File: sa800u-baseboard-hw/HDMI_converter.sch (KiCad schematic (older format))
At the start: 17 parts

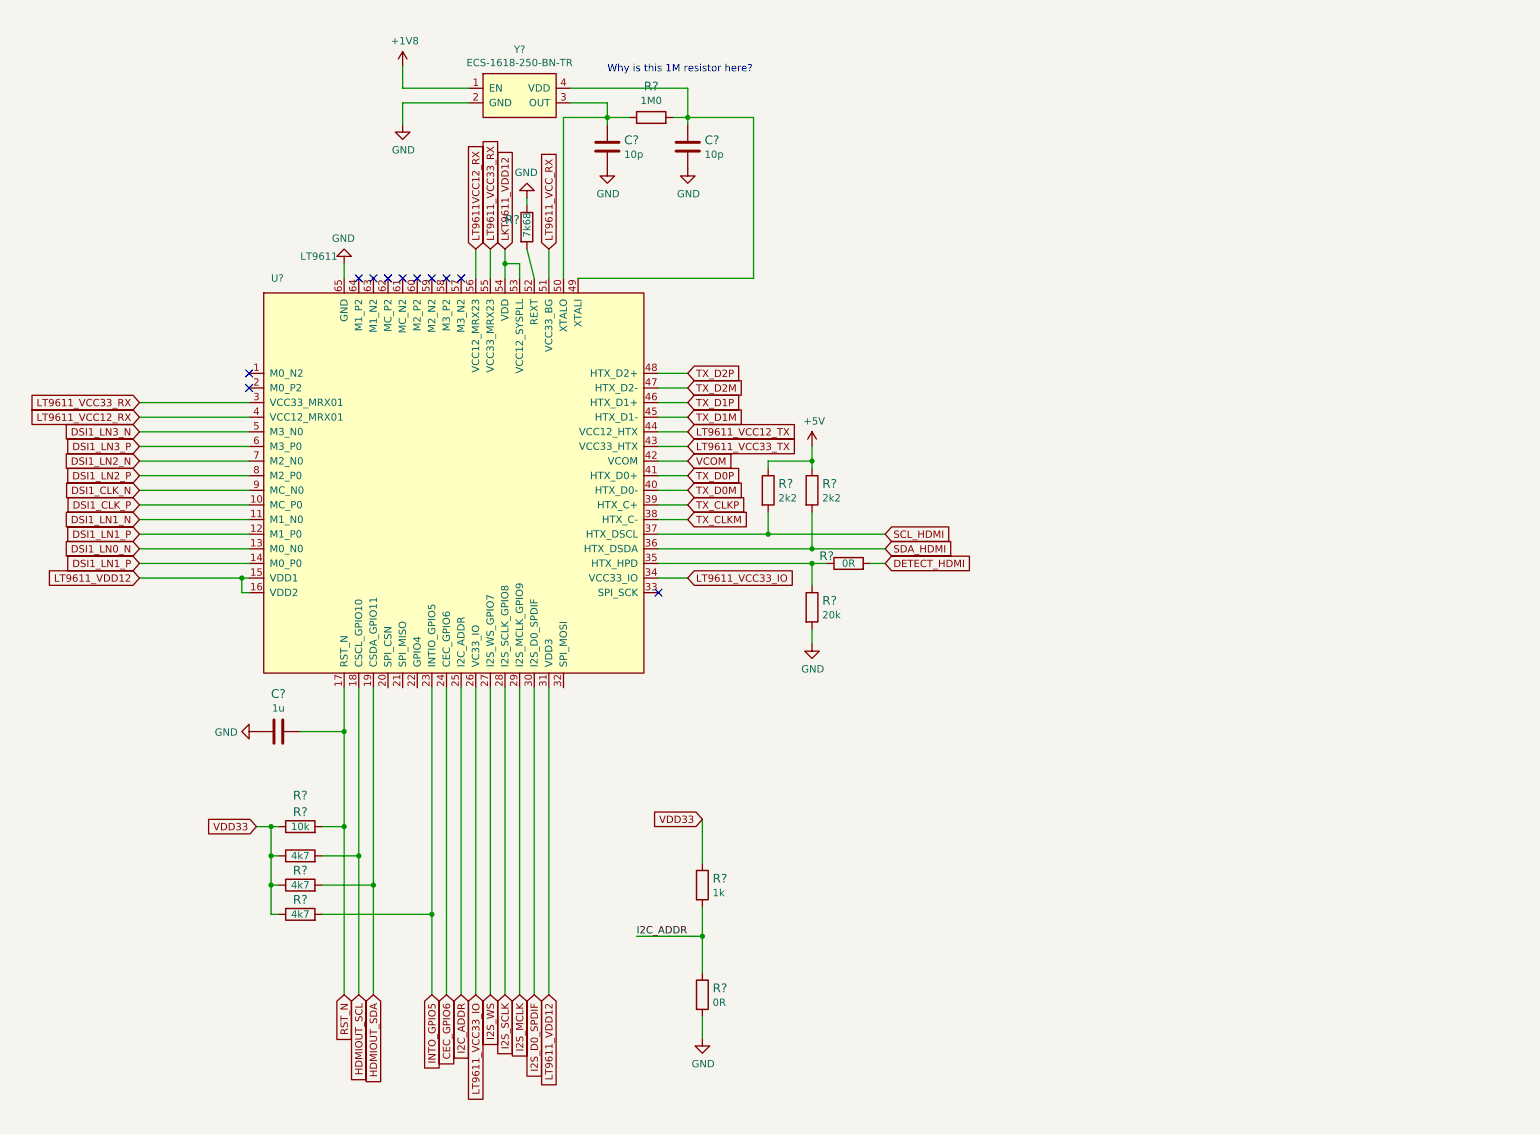
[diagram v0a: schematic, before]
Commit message: added level shifters for I2S, reset, I2C, and GPIO
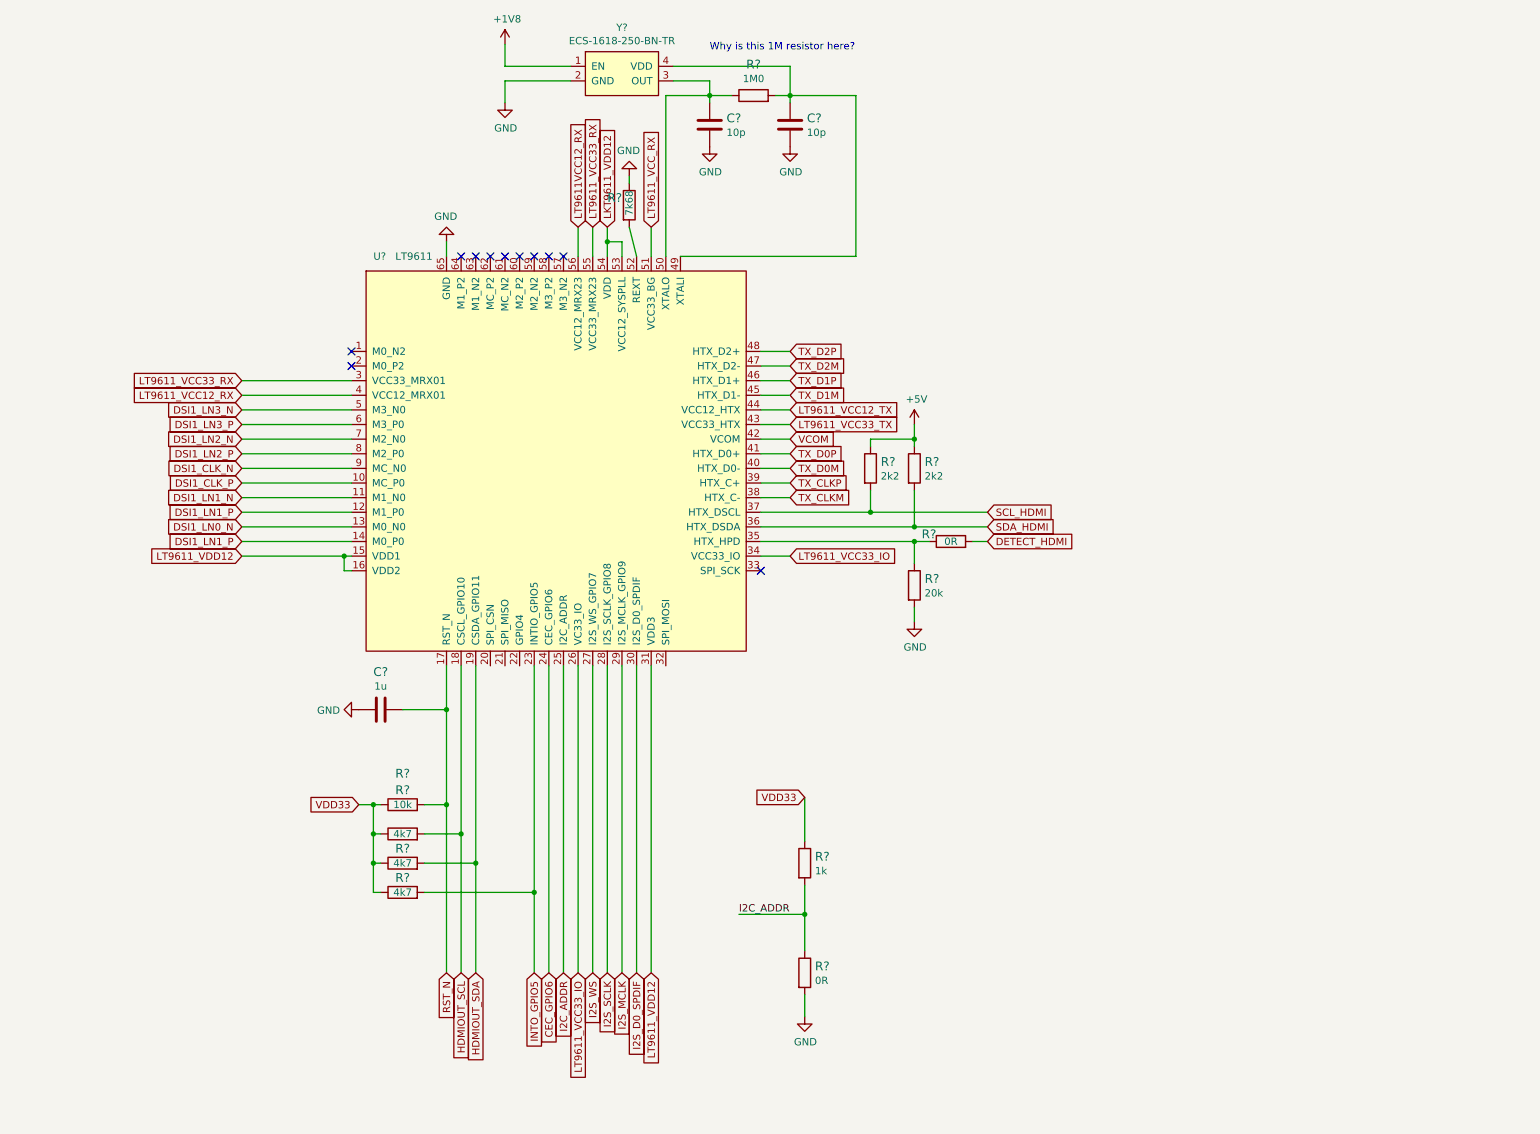
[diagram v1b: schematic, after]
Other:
- moved on the sheet: C?, R?, U?, Y?

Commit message: Review - Add geeral remarks
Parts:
- gave numbers to parts that had none: 17
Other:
- note added: "REMARK: Add components to our repository \n(antmicro-kicad-components)"
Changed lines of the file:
@@
 $EndDescr
 $Comp
-L HDMI:LT9611 U?
+L HDMI:LT9611 U4
 U 1 1 61A0479A
 P 2250 2250
-F 0 "U?" H 2300 2350 50  0000 L CNN
+F 0 "U4" H 2300 2350 50  0000 L CNN
 F 1 "LT9611" H 2450 2350 50  0000 L CNN
 F 2 "" H 1500 1950 50  0001 C CNN
@@
 Connection ~ 2800 5250
 $Comp
-L antmicroCapacitors0402:C_1u_0402 C?
+L antmicroCapacitors0402:C_1u_0402 C31
 U 1 1 61A0B5F1
 P 2350 5250
-F 0 "C?" V 2092 5250 60  0000 C CNN
+F 0 "C31" V 2092 5250 60  0000 C CNN
 F 1 "C_1u_0402" H 2350 5100 60  0001 C CNN
 F 2 "antmicro-footprints:0402-cap" H 2550 5450 60  0001 L CNN
@@
 $EndComp
 $Comp
-L power:GND #PWR?
+L power:GND #PWR0103
 U 1 1 61A0BBF1
 P 2200 5250
-F 0 "#PWR?" H 2200 5000 50  0001 C CNN
+F 0 "#PWR0103" H 2200 5000 50  0001 C CNN
 F 1 "GND" V 2205 5122 50  0000 R CNN
 F 2 "" H 2200 5250 50  0001 C CNN
@@
 VDD33
 $Comp
-L antmicroResistors0603:R_10k_0603 R?
+L antmicroResistors0603:R_10k_0603 R32
 U 1 1 61A0DBB2
 P 2500 5900
-F 0 "R?" H 2500 6113 60  0000 C CNN
+F 0 "R32" H 2500 6113 60  0000 C CNN
 F 1 "R_10k_0603" H 2500 5750 60  0001 C CNN
 F 2 "antmicro-footprints:0603-res" H 2700 6100 60  0001 L CNN
@@
 	3000 6300 2650 6300
 $Comp
-L antmicroResistors0402:R_4k7_0402 R?
+L antmicroResistors0402:R_4k7_0402 R33
 U 1 1 61A1095E
 P 2500 6100
-F 0 "R?" H 2500 6400 60  0000 C CNN
+F 0 "R33" H 2500 6400 60  0000 C CNN
 F 1 "R_4k7_0402" H 2500 5950 60  0001 C CNN
 F 2 "antmicro-footprints:0402-res" H 2700 6300 60  0001 L CNN
@@
 $EndComp
 $Comp
-L antmicroResistors0402:R_4k7_0402 R?
+L antmicroResistors0402:R_4k7_0402 R34
 U 1 1 61A10E15
 P 2500 6300
-F 0 "R?" H 2500 6400 60  0000 C CNN
+F 0 "R34" H 2500 6400 60  0000 C CNN
 F 1 "R_4k7_0402" H 2500 6150 60  0001 C CNN
 F 2 "antmicro-footprints:0402-res" H 2700 6500 60  0001 L CNN
@@
 $EndComp
 $Comp
-L antmicroResistors0402:R_4k7_0402 R?
+L antmicroResistors0402:R_4k7_0402 R35
 U 1 1 61A1104E
 P 2500 6500
-F 0 "R?" H 2500 6600 60  0000 C CNN
+F 0 "R35" H 2500 6600 60  0000 C CNN
 F 1 "R_4k7_0402" H 2500 6350 60  0001 C CNN
 F 2 "antmicro-footprints:0402-res" H 2700 6700 60  0001 L CNN
@@
 	5250 5850 5250 6150
 $Comp
-L antmicroResistors0402:R_1k_0402 R?
+L antmicroResistors0402:R_1k_0402 R38
 U 1 1 61A23865
 P 5250 6300
-F 0 "R?" V 5205 6370 60  0000 L CNN
+F 0 "R38" V 5205 6370 60  0000 L CNN
 F 1 "R_1k_0402" H 5250 6150 60  0001 C CNN
 F 2 "antmicro-footprints:0402-res" H 5450 6500 60  0001 L CNN
@@
 Connection ~ 5250 6650
 $Comp
-L antmicroResistors0402:R_0R_0402 R?
+L antmicroResistors0402:R_0R_0402 R39
 U 1 1 61A265AB
 P 5250 7050
-F 0 "R?" V 5205 7120 60  0000 L CNN
+F 0 "R39" V 5205 7120 60  0000 L CNN
 F 1 "R_0R_0402" H 5250 6900 60  0001 C CNN
 F 2 "antmicro-footprints:0402-res" H 5450 7250 60  0001 L CNN
@@
 	5250 7200 5250 7350
 $Comp
-L power:GND #PWR?
+L power:GND #PWR0104
 U 1 1 61A2732C
 P 5250 7350
-F 0 "#PWR?" H 5250 7100 50  0001 C CNN
+F 0 "#PWR0104" H 5250 7100 50  0001 C CNN
 F 1 "GND" H 5255 7177 50  0000 C CNN
 F 2 "" H 5250 7350 50  0001 C CNN
@@
 	5700 3900 6500 3900
 $Comp
-L antmicroResistors0402:R_2k2_0402 R?
+L antmicroResistors0402:R_2k2_0402 R40
 U 1 1 61A367B5
 P 5700 3600
-F 0 "R?" V 5655 3670 60  0000 L CNN
+F 0 "R40" V 5655 3670 60  0000 L CNN
 F 1 "R_2k2_0402" H 5700 3450 60  0001 C CNN
 F 2 "antmicro-footprints:0402-res" H 5900 3800 60  0001 L CNN
@@
 $EndComp
 $Comp
-L antmicroResistors0402:R_2k2_0402 R?
+L antmicroResistors0402:R_2k2_0402 R41
 U 1 1 61A36C6F
 P 6000 3600
-F 0 "R?" V 5955 3670 60  0000 L CNN
+F 0 "R41" V 5955 3670 60  0000 L CNN
 F 1 "R_2k2_0402" H 6000 3450 60  0001 C CNN
 F 2 "antmicro-footprints:0402-res" H 6200 3800 60  0001 L CNN
@@
 Connection ~ 6000 3400
 $Comp
-L power:+5V #PWR?
+L power:+5V #PWR0106
 U 1 1 61A3A044
 P 6000 3300
-F 0 "#PWR?" H 6000 3150 50  0001 C CNN
+F 0 "#PWR0106" H 6000 3150 50  0001 C CNN
 F 1 "+5V" H 6015 3473 50  0000 C CNN
 F 2 "" H 6000 3300 50  0001 C CNN
@@
 $EndComp
 $Comp
-L antmicroResistors0402:R_0R_0402 R?
+L antmicroResistors0402:R_0R_0402 R43
 U 1 1 61A3ACDD
 P 6250 4100
-F 0 "R?" H 6100 4150 60  0000 C CNN
+F 0 "R43" H 6100 4150 60  0000 C CNN
 F 1 "R_0R_0402" H 6250 3950 60  0001 C CNN
 F 2 "antmicro-footprints:0402-res" H 6450 4300 60  0001 L CNN
@@
 	6000 4100 6100 4100
 $Comp
-L antmicroResistors0402:R_20k_0402 R?
+L antmicroResistors0402:R_20k_0402 R42
 U 1 1 61A3C72D
 P 6000 4400
-F 0 "R?" V 5955 4470 60  0000 L CNN
+F 0 "R42" V 5955 4470 60  0000 L CNN
 F 1 "R_20k_0402" H 6000 4250 60  0001 C CNN
 F 2 "antmicro-footprints:0402-res" H 6200 4600 60  0001 L CNN
@@
 $EndComp
 $Comp
-L power:GND #PWR?
+L power:GND #PWR0112
 U 1 1 61A3D3AB
 P 6000 4650
-F 0 "#PWR?" H 6000 4400 50  0001 C CNN
+F 0 "#PWR0112" H 6000 4400 50  0001 C CNN
 F 1 "GND" H 6005 4477 50  0000 C CNN
 F 2 "" H 6000 4650 50  0001 C CNN
@@
 	5150 3100 4950 3100
 $Comp
-L power:GND #PWR?
+L power:GND #PWR0113
 U 1 1 61A49B07
 P 2800 2050
-F 0 "#PWR?" H 2800 1800 50  0001 C CNN
+F 0 "#PWR0113" H 2800 1800 50  0001 C CNN
 F 1 "GND" H 2805 1877 50  0000 C CNN
 F 2 "" H 2800 2050 50  0001 C CNN
@@
 NoConn ~ 4950 4300
 $Comp
-L antmicroResistors0603:R_7k68_0603 R?
+L antmicroResistors0603:R_7k68_0603 R36
 U 1 1 61A5CF19
 P 4050 1800
-F 0 "R?" V 4000 1650 60  0000 L CNN
+F 0 "R36" V 4000 1650 60  0000 L CNN
 F 1 "R_7k68_0603" H 4050 1650 60  0001 C CNN
 F 2 "antmicro-footprints:0603-res" H 4250 2000 60  0001 L CNN
@@
 $EndComp
 $Comp
-L power:GND #PWR?
+L power:GND #PWR0114
 U 1 1 61A5D5F6
 P 4050 1600
-F 0 "#PWR?" H 4050 1350 50  0001 C CNN
+F 0 "#PWR0114" H 4050 1350 50  0001 C CNN
 F 1 "GND" H 4055 1427 50  0000 C CNN
 F 2 "" H 4050 1600 50  0001 C CNN
@@
 P 3200 1100
 AR Path="/618E716E/61A80E9F" Ref="#PWR?"  Part="1"
-AR Path="/6197686D/61A80E9F" Ref="#PWR?"  Part="1"
-F 0 "#PWR?" H 3200 850 50  0001 C CNN
+AR Path="/6197686D/61A80E9F" Ref="#PWR0115"  Part="1"
+F 0 "#PWR0115" H 3200 850 50  0001 C CNN
 F 1 "GND" H 3205 927 50  0000 C CNN
 F 2 "" H 3200 1100 50  0001 C CNN
@@
 P 3200 700
 AR Path="/618E716E/61A80E97" Ref="#PWR?"  Part="1"
-AR Path="/6197686D/61A80E97" Ref="#PWR?"  Part="1"
-F 0 "#PWR?" H 3200 550 50  0001 C CNN
+AR Path="/6197686D/61A80E97" Ref="#PWR0116"  Part="1"
+F 0 "#PWR0116" H 3200 550 50  0001 C CNN
 F 1 "+1V8" H 3215 873 50  0000 C CNN
 F 2 "" H 3200 700 50  0001 C CNN
@@
 P 3750 750
 AR Path="/618E716E/61A80E8F" Ref="Y?"  Part="1"
-AR Path="/6197686D/61A80E8F" Ref="Y?"  Part="1"
-F 0 "Y?" H 4000 915 50  0000 C CNN
+AR Path="/6197686D/61A80E8F" Ref="Y2"  Part="1"
+F 0 "Y2" H 4000 915 50  0000 C CNN
 F 1 "ECS-1618-250-BN-TR" H 4000 824 50  0000 C CNN
 F 2 "" H 3950 800 50  0001 C CNN
@@
 P 4600 1250
 AR Path="/618E716E/61A80EAA" Ref="C?"  Part="1"
-AR Path="/6197686D/61A80EAA" Ref="C?"  Part="1"
-F 0 "C?" H 4715 1295 60  0000 L CNN
+AR Path="/6197686D/61A80EAA" Ref="C32"  Part="1"
+F 0 "C32" H 4715 1295 60  0000 L CNN
 F 1 "C_10p_0402" H 4600 1100 60  0001 C CNN
 F 2 "antmicro-footprints:0402-cap" H 4800 1450 60  0001 L CNN
@@
 P 4600 1400
 AR Path="/618E716E/61A80EB0" Ref="#PWR?"  Part="1"
-AR Path="/6197686D/61A80EB0" Ref="#PWR?"  Part="1"
-F 0 "#PWR?" H 4600 1150 50  0001 C CNN
+AR Path="/6197686D/61A80EB0" Ref="#PWR0117"  Part="1"
+F 0 "#PWR0117" H 4600 1150 50  0001 C CNN
 F 1 "GND" H 4605 1227 50  0000 C CNN
 F 2 "" H 4600 1400 50  0001 C CNN
@@
 P 5150 1250
 AR Path="/618E716E/61A80EBB" Ref="C?"  Part="1"
-AR Path="/6197686D/61A80EBB" Ref="C?"  Part="1"
-F 0 "C?" H 5265 1295 60  0000 L CNN
+AR Path="/6197686D/61A80EBB" Ref="C33"  Part="1"
+F 0 "C33" H 5265 1295 60  0000 L CNN
 F 1 "C_10p_0402" H 5150 1100 60  0001 C CNN
 F 2 "antmicro-footprints:0402-cap" H 5350 1450 60  0001 L CNN
@@
 P 5150 1400
 AR Path="/618E716E/61A80EC1" Ref="#PWR?"  Part="1"
-AR Path="/6197686D/61A80EC1" Ref="#PWR?"  Part="1"
-F 0 "#PWR?" H 5150 1150 50  0001 C CNN
+AR Path="/6197686D/61A80EC1" Ref="#PWR0118"  Part="1"
+F 0 "#PWR0118" H 5150 1150 50  0001 C CNN
 F 1 "GND" H 5155 1227 50  0000 C CNN
 F 2 "" H 5150 1400 50  0001 C CNN
@@
 P 4900 1050
 AR Path="/618E716E/61A80ECC" Ref="R?"  Part="1"
-AR Path="/6197686D/61A80ECC" Ref="R?"  Part="1"
-F 0 "R?" H 4900 1263 60  0000 C CNN
+AR Path="/6197686D/61A80ECC" Ref="R37"  Part="1"
+F 0 "R37" H 4900 1263 60  0000 C CNN
 F 1 "R_1M0_0402" H 4900 900 60  0001 C CNN
 F 2 "antmicro-footprints:0402-res" H 5100 1250 60  0001 L CNN
@@
 Text GLabel 4200 7050 3    50   Input ~ 0
 LT9611_VDD12
+Text Notes 525  2275 0    50   ~ 0
+REMARK: Add components to our repository \n(antmicro-kicad-components)
 $EndSCHEMATC
